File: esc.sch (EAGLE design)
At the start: 61 parts, among them IC1 78L05F, Q1 16 MHz, T1 IRFR1205, T2 IRFR1205, T3 IRFR1205, T4 IRFR1205, T5 IRFR1205, T6 IRFR1205, U1 ATMEGA48-20AU

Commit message: ppm via, phase c fixed
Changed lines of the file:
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@@
-</segment>
-</net>
-<net name="N$8" class="0">
-<segment>
-<pinref part="T6" gate="G$1" pin="S"/>
-<wire x1="213.36" y1="-15.24" x2="213.36" y2="-22.86" width="0.1524" layer="91"/>
-<pinref part="T4" gate="G$1" pin="S"/>
-<wire x1="213.36" y1="40.64" x2="213.36" y2="33.02" width="0.1524" layer="91"/>
-<pinref part="T2" gate="G$1" pin="S"/>
-<wire x1="213.36" y1="96.52" x2="213.36" y2="88.9" width="0.1524" layer="91"/>
-<wire x1="213.36" y1="88.9" x2="233.68" y2="88.9" width="0.1524" layer="91"/>
-<wire x1="233.68" y1="88.9" x2="233.68" y2="33.02" width="0.1524" layer="91"/>
-<wire x1="233.68" y1="33.02" x2="233.68" y2="-22.86" width="0.1524" layer="91"/>
-<wire x1="213.36" y1="33.02" x2="233.68" y2="33.02" width="0.1524" layer="91"/>
-<junction x="233.68" y="33.02"/>
-<wire x1="213.36" y1="-22.86" x2="233.68" y2="-22.86" width="0.1524" layer="91"/>
-<pinref part="R9" gate="G$1" pin="1"/>
-<wire x1="233.68" y1="-30.48" x2="233.68" y2="-27.94" width="0.1524" layer="91"/>
-<wire x1="233.68" y1="-27.94" x2="233.68" y2="-22.86" width="0.1524" layer="91"/>
-<wire x1="233.68" y1="-27.94" x2="241.3" y2="-27.94" width="0.1524" layer="91"/>
-<wire x1="241.3" y1="-27.94" x2="241.3" y2="-38.1" width="0.1524" layer="91"/>
-<junction x="233.68" y="-27.94"/>
-<pinref part="R10" gate="G$1" pin="2"/>
 </segment>
 </net>
@@
 </segment>
 </net>
+<net name="N$7" class="0">
+<segment>
+<pinref part="T6" gate="G$1" pin="S"/>
+<wire x1="213.36" y1="-15.24" x2="213.36" y2="-22.86" width="0.1524" layer="91"/>
+<pinref part="T4" gate="G$1" pin="S"/>
+<wire x1="213.36" y1="40.64" x2="213.36" y2="33.02" width="0.1524" layer="91"/>
+<pinref part="T2" gate="G$1" pin="S"/>
+<wire x1="213.36" y1="96.52" x2="213.36" y2="88.9" width="0.1524" layer="91"/>
+<wire x1="213.36" y1="88.9" x2="233.68" y2="88.9" width="0.1524" layer="91"/>
+<wire x1="233.68" y1="88.9" x2="233.68" y2="33.02" width="0.1524" layer="91"/>
+<wire x1="233.68" y1="33.02" x2="233.68" y2="-22.86" width="0.1524" layer="91"/>
+<wire x1="233.68" y1="-22.86" x2="233.68" y2="-27.94" width="0.1524" layer="91"/>
+<wire x1="213.36" y1="33.02" x2="233.68" y2="33.02" width="0.1524" layer="91"/>
+<junction x="233.68" y="33.02"/>
+<pinref part="R9" gate="G$1" pin="1"/>
+<wire x1="233.68" y1="-30.48" x2="233.68" y2="-27.94" width="0.1524" layer="91"/>
+<wire x1="233.68" y1="-27.94" x2="241.3" y2="-27.94" width="0.1524" layer="91"/>
+<wire x1="241.3" y1="-27.94" x2="241.3" y2="-38.1" width="0.1524" layer="91"/>
+<junction x="233.68" y="-27.94"/>
+<pinref part="R10" gate="G$1" pin="2"/>
+<wire x1="213.36" y1="-22.86" x2="233.68" y2="-22.86" width="0.1524" layer="91"/>
+<junction x="233.68" y="-22.86"/>
+</segment>
+</net>

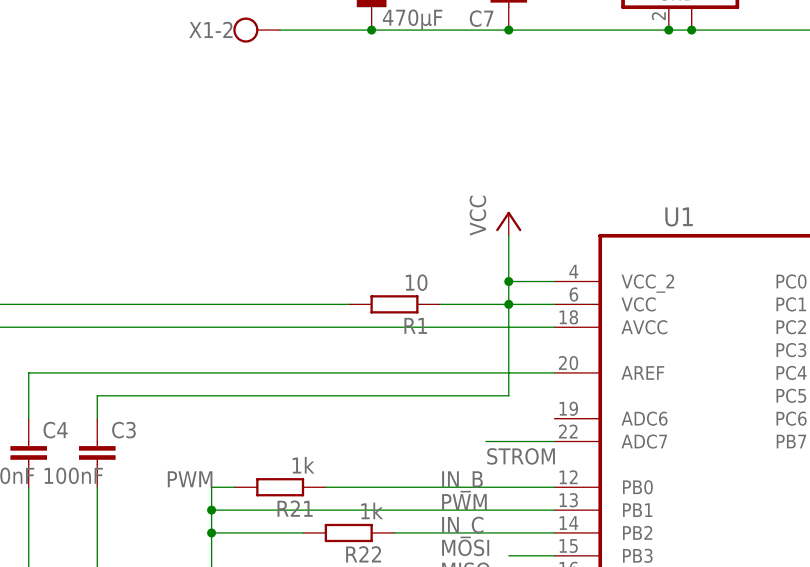
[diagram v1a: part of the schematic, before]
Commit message: Added value to r1 and tRestrict under Quarz
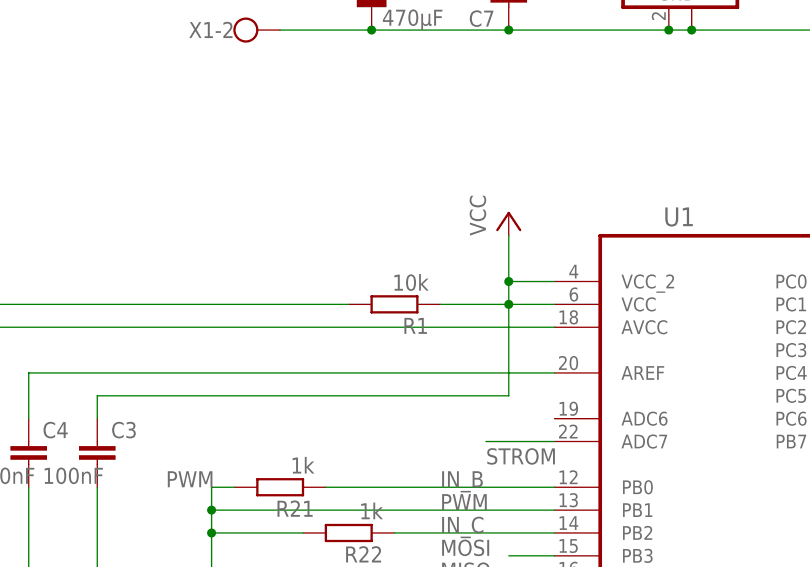
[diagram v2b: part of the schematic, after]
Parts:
- R1: value 10 -> 10k
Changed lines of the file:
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@@
 <part name="C4" library="rcl" deviceset="C-EU" device="C1206" value="100nF"/>
 <part name="C5" library="rcl" deviceset="C-EU" device="C1206" value="100nF"/>
-<part name="R1" library="rcl" deviceset="R-EU_" device="R1206" value="10"/>
+<part name="R1" library="rcl" deviceset="R-EU_" device="R1206" value="10k"/>
 <part name="GND2" library="supply1" deviceset="GND" device=""/>
 <part name="R2" library="rcl" deviceset="R-EU_" device="R1206" value="10k"/>
